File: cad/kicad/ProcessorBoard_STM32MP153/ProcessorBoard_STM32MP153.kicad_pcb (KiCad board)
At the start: 6 copper layers, 49.7 x 49.6 mm, 140 parts, among them IC301 STPMIC1BPQR, J301 Conn_01x01_Pin, J501 SFP, Q501 MMBTA92, Q502 MMBT5551L, Q503 MMBT5551L, Q504 MMBT5551L, Q505 MMBT5551L, Q506 MMBTA92, Q507 MMBT5551L, Q508 MMBTA92, Q509 MMBTA92, SW201 SW_DIP_x03, U201 STM32MP153CACx, U402 W97AH6NBVAxx, U501 DSC6101HL3B-025.0000, U502 TXS0102DCU, X201 ECS-3225MVQ-240-CN-TR, X501 RTL8211FS(I)-xx-xx

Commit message: boo womp 10000
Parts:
- moved R207 104.9 mm to (182.1, 76.7)
- moved C504 97.3 mm to (185.9, 75.8)
- moved C601 93.8 mm to (182.1, 69.1)
- moved C602 93.8 mm to (182.1, 71.6)
- moved L601 93.8 mm to (186.9, 69.8)
- moved C603 93.8 mm to (182.1, 74.2)
- moved R601 92.6 mm to (182.1, 79.2)
- moved R602 92.6 mm to (182.1, 81.7)
- moved U601 13.1 mm to (186.0, 73.3)

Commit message: found reference schematic :he he he ha:
coincidence using the same chip !? am i tweaking or tamale-n brap
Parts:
- removed C505: 100n, Capacitor_SMD:C_0402_1005Metric_Pad0.74x0.62mm_HandSolder
- removed C601, C602, C603: 10u, Capacitor_SMD:C_0603_1608Metric_Pad1.08x0.95mm_HandSolder
- removed L601: 1u, Inductor_SMD:L_1008_2520Metric_Pad1.43x2.20mm_HandSolder
- removed Q501, Q506, Q508, Q509: MMBTA92, Package_TO_SOT_SMD:SOT-23
- removed Q502, Q503, Q504, Q505, Q507: MMBT5551L, Package_TO_SOT_SMD:SOT-23
- removed R504: 240, Capacitor_SMD:C_0402_1005Metric_Pad0.74x0.62mm_HandSolder
- removed R601: 45.3k, Resistor_SMD:R_0603_1608Metric_Pad0.98x0.95mm_HandSolder
- removed R602: 10k, Resistor_SMD:R_0603_1608Metric_Pad0.98x0.95mm_HandSolder
- removed U501: DSC6101HL3B-025.0000, Package_LGA:VLGA-4_2x2.5mm_P1.65mm
- removed U601: ~, Package_TO_SOT_SMD:SOT-563
- added C514: 4.7u, Capacitor_SMD:C_0402_1005Metric_Pad0.74x0.62mm_HandSolder, F.Cu at (182.4, 90.2)
- added C515: 4.7u, Capacitor_SMD:C_0402_1005Metric_Pad0.74x0.62mm_HandSolder, F.Cu at (142.1, 52.1)
- added C516: 4.7u, Capacitor_SMD:C_0402_1005Metric_Pad0.74x0.62mm_HandSolder, F.Cu at (142.1, 54.1)
- added C517: 1n, Capacitor_SMD:C_0402_1005Metric_Pad0.74x0.62mm_HandSolder, F.Cu at (182.4, 92.2)
- added D502: LED_ABGR, LED_SMD:LED_ASMB-KTF0-0A306, F.Cu at (154.9, 50.9)
- added D503: LED_ABGR, LED_SMD:LED_ASMB-KTF0-0A306, F.Cu at (154.9, 54.5)
- added R515: 330, Resistor_SMD:R_0603_1608Metric_Pad0.98x0.95mm_HandSolder, F.Cu at (150.6, 52.9)
- added R516: 240, Capacitor_SMD:C_0402_1005Metric_Pad0.74x0.62mm_HandSolder, F.Cu at (142.1, 58.0)
- added R517: 240, Capacitor_SMD:C_0402_1005Metric_Pad0.74x0.62mm_HandSolder, F.Cu at (142.1, 60.0)
- added R518: 10k, Resistor_SMD:R_0603_1608Metric_Pad0.98x0.95mm_HandSolder, F.Cu at (150.6, 55.4)
- added R519: 5.6k, Resistor_SMD:R_0805_2012Metric_Pad1.20x1.40mm_HandSolder, F.Cu at (146.1, 59.5)
- added R520: 0, Resistor_SMD:R_0603_1608Metric, B.Cu at (169.3, 84.0)
- added U503: SN74LVC07AD, __WM_Local:D0014A_M, F.Cu at (145.2, 43.7)
- added U504: SN74LVC07AD, __WM_Local:D0014A_M, F.Cu at (154.6, 43.7)
- C233, C501, R202, R203, R204, X201: moved to B.Cu
- L502, L503: footprint Inductor_SMD:L_1008_2520Metric_Pad1.43x2.20mm_HandSolder -> Inductor_SMD:L_0805_2012Metric_Pad1.05x1.20mm_HandSolder
- R501: value 5.6k -> 100; footprint Resistor_SMD:R_0805_2012Metric_Pad1.20x1.40mm_HandSolder -> Resistor_SMD:R_0402_1005Metric
- R503: value 330 -> 5.6k; footprint Resistor_SMD:R_0603_1608Metric_Pad0.98x0.95mm_HandSolder -> Resistor_SMD:R_0805_2012Metric_Pad1.20x1.40mm_HandSolder
- R505: value 240 -> 2.49k; footprint Capacitor_SMD:C_0402_1005Metric_Pad0.74x0.62mm_HandSolder -> Resistor_SMD:R_0603_1608Metric_Pad0.98x0.95mm_HandSolder
- moved R502 104.7 mm to (146.1, 50.6)
- moved R202 95.5 mm to (174.1, 86.8)
- moved C502 92.6 mm to (176.5, 78.6), turned to -45 degrees
- moved R505 92.4 mm to (150.6, 50.4)
- moved C233 92.3 mm to (171.7, 89.1), turned to -90 degrees
- moved R503 89.5 mm to (146.1, 53.6)
- moved L501 88.4 mm to (173.8, 81.2), turned to 45 degrees
- moved C501 84.1 mm to (169.7, 85.3), turned to 180 degrees
- moved C503 82.7 mm to (173.1, 88.8)
- moved R501 66.3 mm to (165.8, 80.6), turned to 45 degrees
- moved R203 42.0 mm to (170.4, 90.4), turned to 90 degrees
- moved R204 41.0 mm to (171.7, 86.8), turned to -90 degrees
- moved X201 40.0 mm to (174.2, 89.5), turned to 180 degrees
- moved L503 13.9 mm to (159.5, 53.3)
- moved L502 12.9 mm to (159.5, 50.5)
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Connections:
- net Net-(C502-Pad1) renamed /SPF/ir_1v0
- net Net-(J501-TD+) renamed /SPF/SERDES_O_P
- net Net-(J501-TD-) renamed /SPF/SERDES_O_N
- net Net-(X501-REG_OUT) renamed /SPF/ir_out
- J501 pad 12: Net-(J501-RD-) -> /SPF/SERDES_I_N
- J501 pad 13: Net-(J501-RD+) -> /SPF/SERDES_I_P
- R501 pad 1: GND -> /SPF/SERDES_I_N
- R501 pad 2: /SPF/LED_{1} -> /SPF/SERDES_I_P
- R502 pad 1: /SPF/sfp.3v3 -> /SPF/LED_{2}
- R502 pad 2: /SPF/LED_{2} -> /SPF/sfp.3v3
- R503 pad 1: Net-(Q501-E) -> /sfp.rxd1
- R503 pad 2: Net-(D501-RK) -> /SPF/sfp.V_{io}
- R505 pad 1: Net-(Q501-E) -> Net-(X501-RSET)
- R505 pad 2: Net-(D501-BK) -> GND
- U201 pad AA1: unconnected-(U201-PG14-PadAA1) -> /sfp.txd1
- U201 pad AA2: unconnected-(U201-PG13-PadAA2) -> /sfp.txd0
- U201 pad AA4: unconnected-(U201-PA1-PadAA4) -> /sfp.rxc
- U201 pad AA6: unconnected-(U201-PC1-PadAA6) -> /sfp.mdc
- U201 pad AB2: unconnected-(U201-PG4-PadAB2) -> /sfp.txc
- U201 pad AB7: unconnected-(U201-PC5-PadAB7) -> /sfp.rxd1
- U201 pad AB8: unconnected-(U201-PA7-PadAB8) -> /sfp.rxctl
- U201 pad AC3: unconnected-(U201-PA2-PadAC3) -> /sfp.mdio
- U201 pad AC7: unconnected-(U201-PC4-PadAC7) -> /sfp.rxd0
- U201 pad K4: unconnected-(U201-PG12-PadK4) -> /sfp.phy.int#
- U201 pad W4: unconnected-(U201-PH7-PadW4) -> /sfp.rxd3
- U201 pad Y1: unconnected-(U201-PE2-PadY1) -> /sfp.txd3
- U201 pad Y11: unconnected-(U201-PH6-PadY11) -> /sfp.rxd2
- U201 pad Y2: unconnected-(U201-PC2-PadY2) -> /sfp.txd2
- U201 pad Y6: unconnected-(U201-PG5-PadY6) -> /sfp.phymac_frclk_125
- U201 pad Y7: unconnected-(U201-PG11-PadY7) -> /sfp.txctl
- U201 pad Y8: unconnected-(U201-PB5-PadY8) -> /sfp.macphy_clk_25
- X501 pad 13: unconnected-(X501-PHY_RSTB#-Pad13) -> /sfp.phy.reset#
- X501 pad 14: unconnected-(X501-MDC-Pad14) -> /sfp.mdc
- X501 pad 15: unconnected-(X501-MDIO-Pad15) -> /sfp.mdio
- X501 pad 16: unconnected-(X501-TXD_{3}-Pad16) -> /sfp.txd3
- X501 pad 17: unconnected-(X501-TXD_{2}-Pad17) -> /sfp.txd2
- X501 pad 18: unconnected-(X501-TXD_{1}-Pad18) -> /sfp.txd1
- X501 pad 19: unconnected-(X501-TXD_{0}-Pad19) -> /sfp.txd0
- X501 pad 20: unconnected-(X501-TXCTL-Pad20) -> /sfp.txctl
- X501 pad 21: unconnected-(X501-TXCLK-Pad21) -> /sfp.txc
- X501 pad 23: unconnected-(X501-CFG_{mode2}-Pad23) -> /sfp.rxd3
- X501 pad 24: unconnected-(X501-CFG_{mode1}-Pad24) -> /sfp.rxd2
- X501 pad 25: unconnected-(X501-CFG_{mode0}-Pad25) -> /sfp.rxd1
- X501 pad 26: unconnected-(X501-RXDLY-Pad26) -> /sfp.rxd0
- X501 pad 27: unconnected-(X501-PHYAD_{2}-Pad27) -> /sfp.rxctl
- X501 pad 28: unconnected-(X501-PHYAD_{1}-Pad28) -> /sfp.rxc
- X501 pad 29: unconnected-(X501-DV_{dd}_RG-Pad29) -> /SPF/sfp.V_{io}
- X501 pad 33: unconnected-(X501-PTP_CLKIN/GPIO_{0}-Pad33) -> Net-(X501-PTP_CLKIN/GPIO_{0})
- X501 pad 34: unconnected-(X501-INTB/PMEB-Pad34) -> /sfp.phy.int#
- X501 pad 35: unconnected-(X501-PHYAD_{0}-Pad35) -> /SPF/LED_{0}
- X501 pad 38: Net-(J501-RD+) -> /SPF/SERDES_I_P
- X501 pad 39: Net-(J501-RD-) -> /SPF/SERDES_I_N
- X501 pad 44: unconnected-(X501-CLKOUT-Pad44) -> /sfp.phymac_frclk_125
- X501 pad 46: /SPF/xtal_out -> /sfp.macphy_clk_25
- X501 pad 48: /SPF/reset -> Net-(X501-RSET)
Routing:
- net Net-(X201-V_{dd}): track 0.00 -> 2.61 mm
- net Net-(X201-EN): track 0.00 -> 1.81 mm
- net Net-(X501-PTP_CLKIN/GPIO_{0}): track 0.00 -> 0.74 mm
- net GND: track 2.57 -> 2.93 mm, vias 33 -> 35
- net /sfp.rxd0: track 0.00 -> 0.35 mm, vias 0 -> 1
- net /sfp.mdio: track 0.00 -> 0.31 mm, vias 0 -> 1
- net /sfp.phymac_frclk_125: track 0.00 -> 0.31 mm, vias 0 -> 1
- net /sfp.txd1: track 0.00 -> 0.31 mm, vias 0 -> 1
- net /sfp.phy.int#: track 0.00 -> 0.31 mm, vias 0 -> 1
- net /sfp.macphy_clk_25: track 0.00 -> 0.31 mm, vias 0 -> 1
- net /sfp.rxd3: track 0.00 -> 0.31 mm, vias 0 -> 1
- net /sfp.rxc: track 0.00 -> 0.31 mm, vias 0 -> 1
- net /sfp.rxctl: track 0.00 -> 0.31 mm, vias 0 -> 1
- net /sfp.mdc: track 0.00 -> 0.31 mm, vias 0 -> 1
- net /sfp.txd0: track 0.00 -> 0.31 mm, vias 0 -> 1
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
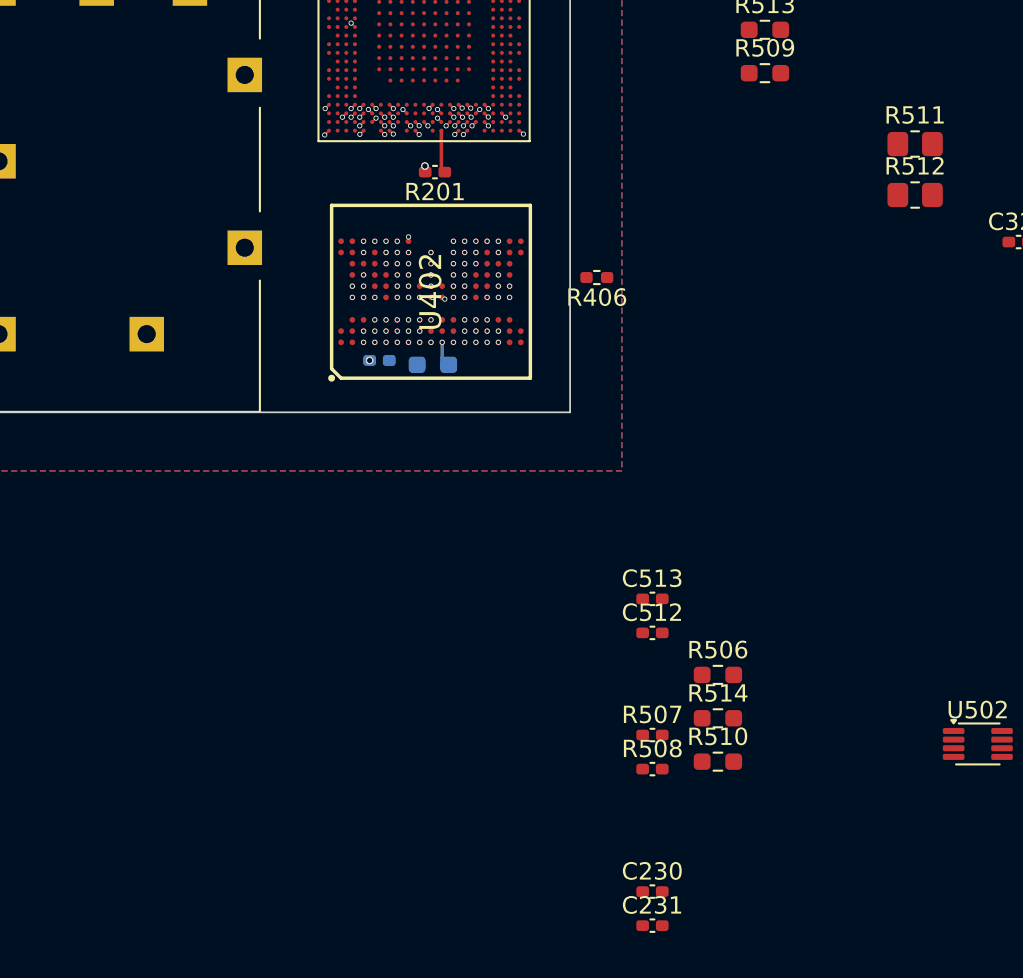
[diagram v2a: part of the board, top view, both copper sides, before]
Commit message: i forgor track spacing :(
need to redo ddr
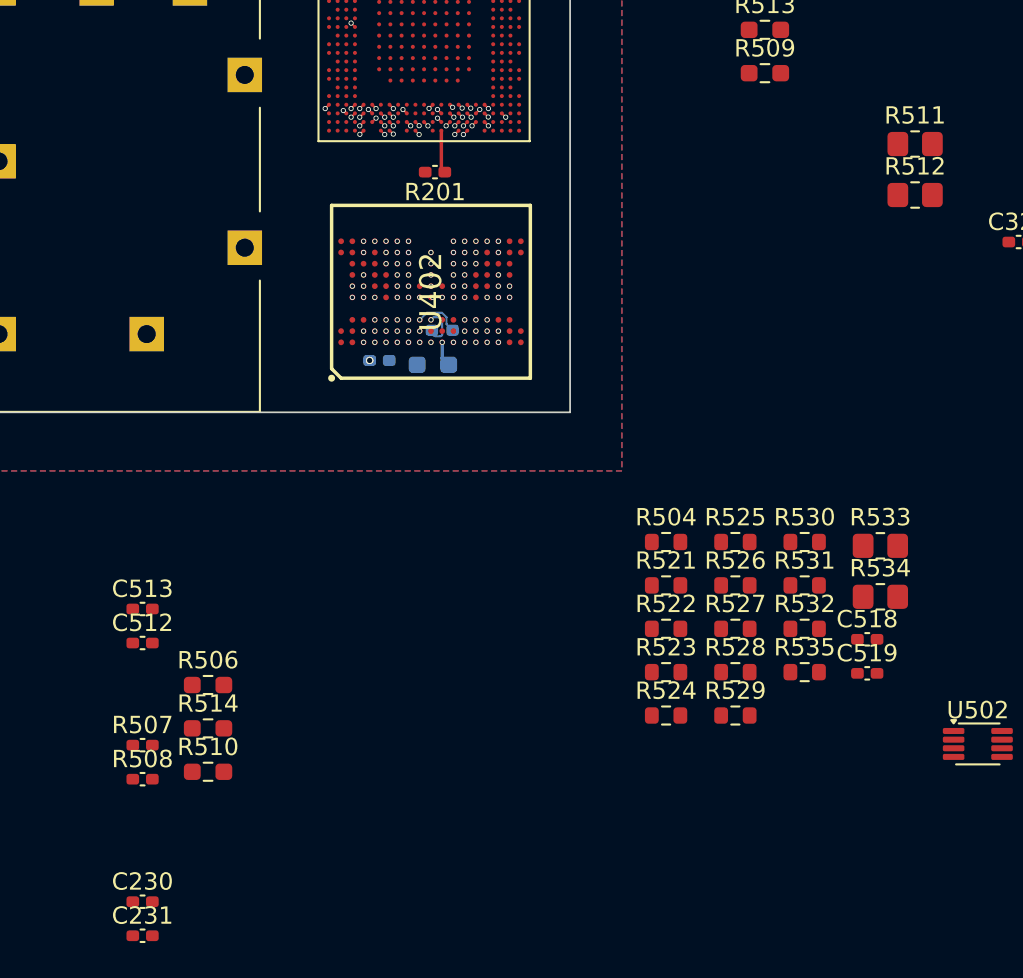
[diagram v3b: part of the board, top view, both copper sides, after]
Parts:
- added C518: 100n, Capacitor_SMD:C_0402_1005Metric_Pad0.74x0.62mm_HandSolder, F.Cu at (197.2, 132.7)
- added C519: 100n, Capacitor_SMD:C_0402_1005Metric_Pad0.74x0.62mm_HandSolder, F.Cu at (197.2, 134.7)
- added R504: 22, Resistor_SMD:R_0603_1608Metric, F.Cu at (185.6, 127.1)
- added R521: 22, Resistor_SMD:R_0603_1608Metric, F.Cu at (185.6, 129.6)
- added R522: 22, Resistor_SMD:R_0603_1608Metric, F.Cu at (185.6, 132.1)
- added R523: 22, Resistor_SMD:R_0603_1608Metric, F.Cu at (185.6, 134.6)
- added R524: 22, Resistor_SMD:R_0603_1608Metric, F.Cu at (185.6, 137.1)
- added R525: 22, Resistor_SMD:R_0603_1608Metric, F.Cu at (189.6, 127.1)
- added R526: 22, Resistor_SMD:R_0603_1608Metric, F.Cu at (189.6, 129.6)
- added R527: 22, Resistor_SMD:R_0603_1608Metric, F.Cu at (189.6, 132.1)
- added R528: 22, Resistor_SMD:R_0603_1608Metric, F.Cu at (189.6, 134.6)
- added R529: 22, Resistor_SMD:R_0603_1608Metric, F.Cu at (189.6, 137.1)
- added R530: 22, Resistor_SMD:R_0603_1608Metric, F.Cu at (193.6, 127.1)
- added R531: 22, Resistor_SMD:R_0603_1608Metric, F.Cu at (193.6, 129.6)
- added R532: 22, Resistor_SMD:R_0603_1608Metric, F.Cu at (193.6, 132.1)
- added R533: 5.6k, Resistor_SMD:R_0805_2012Metric_Pad1.20x1.40mm_HandSolder, F.Cu at (198.0, 127.3)
- added R534: 5.6k, Resistor_SMD:R_0805_2012Metric_Pad1.20x1.40mm_HandSolder, F.Cu at (198.0, 130.3)
- added R535: 22, Resistor_SMD:R_0603_1608Metric, F.Cu at (193.6, 134.6)
- R406: moved to B.Cu
- moved C230 29.5 mm to (155.3, 147.9)
- moved C231 29.5 mm to (155.3, 149.9)
- moved C512 29.5 mm to (155.3, 132.9)
- moved C513 29.5 mm to (155.3, 131.0)
- moved R506 29.5 mm to (159.1, 135.4)
- moved R507 29.5 mm to (155.3, 138.9)
- moved R508 29.5 mm to (155.3, 140.8)
- moved R510 29.5 mm to (159.1, 140.4)
- moved R514 29.5 mm to (159.1, 137.9)
- moved R406 9.45 mm to (172.6, 114.8), turned to 0 degrees
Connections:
- C501 pad 1: /SPF/sfp.3v3 -> GND
- C501 pad 2: GND -> /3v3
- C503 pad 2: /SPF/sfp.3v3 -> /3v3
- C510 pad 1: /SPF/sfp.3v3 -> /3v3
- C511 pad 1: /SPF/sfp.3v3 -> /3v3
- C512 pad 1: /SPF/sfp.V_{io} -> /V_{dd_IO}
- C513 pad 1: /SPF/sfp.3v3 -> /3v3
- C514 pad 2: /SPF/sfp.V_{io} -> /V_{dd_IO}
- C515 pad 1: /SPF/sfp.3v3 -> /3v3
- C516 pad 1: /SPF/sfp.V_{io} -> /V_{dd_IO}
- C517 pad 2: /SPF/sfp.V_{io} -> /V_{dd_IO}
- D502 pad 1: /SPF/sfp.3v3 -> /3v3
- D503 pad 1: /SPF/sfp.3v3 -> /3v3
- L502 pad 1: /SPF/sfp.3v3 -> /3v3
- L503 pad 1: /SPF/sfp.3v3 -> /3v3
- R502 pad 2: /SPF/sfp.3v3 -> /3v3
- R503 pad 1: /sfp.rxd1 -> /V_{dd_IO}
- R503 pad 2: /SPF/sfp.V_{io} -> Net-(X501-CFG_{mode0})
- R511 pad 2: /SPF/sfp.3v3 -> /3v3
- R512 pad 1: /SPF/sfp.3v3 -> /3v3
- R513 pad 1: /SPF/sfp.3v3 -> /3v3
- R514 pad 1: /SPF/sfp.3v3 -> /3v3
- R518 pad 2: /SPF/sfp.3v3 -> /3v3
- U402 pad E8: /ddr.d12 -> /ddr.d13
- U402 pad F8: /ddr.d10 -> /ddr.d14
- U402 pad F9: /ddr.d13 -> /ddr.d12
- U402 pad G7: /ddr.d14 -> /ddr.d10
- U502 pad 3: /SPF/sfp.V_{io} -> /V_{dd_IO}
- U502 pad 6: /SPF/sfp.V_{io} -> /V_{dd_IO}
- U502 pad 7: /SPF/sfp.3v3 -> /3v3
- U503 pad 14: /SPF/sfp.3v3 -> /3v3
- U504 pad 14: /SPF/sfp.V_{io} -> /V_{dd_IO}
- X501 pad 1: /SPF/sfp.3v3 -> /3v3
- X501 pad 12: /SPF/sfp.3v3 -> /3v3
- X501 pad 14: /sfp.mdc -> Net-(X501-MDC)
- X501 pad 16: /sfp.txd3 -> Net-(X501-TXD_{3})
- X501 pad 17: /sfp.txd2 -> Net-(X501-TXD_{2})
- X501 pad 18: /sfp.txd1 -> Net-(X501-TXD_{1})
- X501 pad 19: /sfp.txd0 -> Net-(X501-TXD_{0})
- X501 pad 20: /sfp.txctl -> Net-(X501-TXCTL)
- X501 pad 21: /sfp.txc -> Net-(X501-TXCLK)
- X501 pad 23: /sfp.rxd3 -> Net-(X501-CFG_{mode2})
- X501 pad 24: /sfp.rxd2 -> Net-(X501-CFG_{mode1})
- X501 pad 25: /sfp.rxd1 -> Net-(X501-CFG_{mode0})
- X501 pad 26: /sfp.rxd0 -> Net-(X501-RXDLY)
- X501 pad 27: /sfp.rxctl -> Net-(X501-PHYAD_{2})
- X501 pad 28: /sfp.rxc -> Net-(X501-PHYAD_{1})
- X501 pad 29: /SPF/sfp.V_{io} -> /V_{dd_IO}
- X501 pad 30: /SPF/sfp.3v3 -> /3v3
- X501 pad 31: /SPF/sfp.3v3 -> /3v3
- X501 pad 44: /sfp.phymac_frclk_125 -> Net-(X501-CLKOUT)
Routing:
- net /ddr.a3: track 24.5 -> 0.31 mm
- net /ddr.d9: track 24.4 -> 0.31 mm
- net /ddr.CSn: track 23.1 -> 0.32 mm
- net /ddr.a1: track 23.1 -> 0.31 mm
- net /ddr.CKE: track 24.6 -> 1.77 mm
- net /ddr.d13: track 23.1 -> 0.30 mm
- net /ddr.a0: track 23.1 -> 0.30 mm
- net /ddr.d8: track 23.0 -> 0.31 mm
- net /ddr.d10: track 23.0 -> 0.31 mm
- net /ddr.CLK_P: track 24.5 -> 2.78 mm
- net /ddr.CLK_N: track 24.4 -> 3.04 mm
- net /ddr.d7: track 24.5 -> 9.34 mm
- net /ddr.d12: track 24.4 -> 10.3 mm
- net /ddr.d0: track 23.0 -> 9.03 mm
- net /ddr.d1: track 24.4 -> 10.4 mm
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
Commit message: ddr shuffle maxxing round 2
mostly hitting the 3w and 4w spacing. one must hope. #hope
ive disabled DRC for optimal routing experience . ching chong over clank ckong any day(until i get the good stuff) has nothing on the sweat shop.
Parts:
- moved R507 80.9 mm to (170.5, 59.4)
- moved R508 80.9 mm to (170.5, 61.4)
- moved R506 80.9 mm to (174.3, 55.9)
- moved R510 80.9 mm to (174.3, 60.9)
- moved R514 80.9 mm to (174.3, 58.4)
- moved C518 57.9 mm to (139.4, 135.4)
- moved C519 57.9 mm to (139.4, 137.4)
- moved R504 57.9 mm to (127.8, 129.8)
- moved R521 57.9 mm to (127.8, 132.3)
- moved R522 57.9 mm to (127.8, 134.8)
- moved R523 57.9 mm to (127.8, 137.3)
- moved R524 57.9 mm to (127.8, 139.8)
- moved R525 57.9 mm to (131.8, 129.8)
- moved R526 57.9 mm to (131.8, 132.3)
- moved R527 57.9 mm to (131.8, 134.8)
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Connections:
- U402 pad E8: /ddr.d13 -> /ddr.d10
- U402 pad F6: /ddr.d15 -> /ddr.d12
- U402 pad F7: /ddr.d11 -> /ddr.d13
- U402 pad F8: /ddr.d14 -> /ddr.d11
- U402 pad F9: /ddr.d12 -> /ddr.d14
- U402 pad G7: /ddr.d10 -> /ddr.d8
- U402 pad G8: /ddr.d8 -> /ddr.d15
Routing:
- net /ddr.d8: track 0.31 -> 27.6 mm
- net /ddr.CKE: track 1.77 -> 27.4 mm
- net /ddr.a0: track 0.30 -> 24.1 mm
- net /ddr.CLK_P: track 2.78 -> 23.0 mm
- net /ddr.CLK_N: track 3.04 -> 22.7 mm
- net /ddr.a1: track 0.31 -> 17.5 mm
- net /ddr.d10: track 0.31 -> 15.5 mm
- net /ddr.CSn: track 0.32 -> 14.1 mm
- net /ddr.a3: track 0.31 -> 13.9 mm
- net /ddr.d9: track 0.31 -> 13.2 mm
- net /ddr.d6: track 14.6 -> 24.0 mm
- net /ddr.d13: track 0.30 -> 8.74 mm
- net /ddr.s1_P: track 12.7 -> 20.5 mm
- net /ddr.s1_N: track 12.8 -> 20.5 mm
- net /ddr.s0_P: track 11.9 -> 19.5 mm
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
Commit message: ddr spaced out 3w 4w binding
smooth as a babys bum or what ever else old folks say
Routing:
- net /ddr.d5: track 11.6 -> 35.2 mm
- net /ddr.d13: track 8.74 -> 31.9 mm
- net /ddr.d7: track 10.4 -> 33.4 mm
- net /ddr.m0: track 10.9 -> 33.5 mm
- net /ddr.d1: track 11.3 -> 32.0 mm
- net /ddr.d3: track 12.9 -> 33.3 mm
- net /ddr.d9: track 13.2 -> 33.4 mm
- net /ddr.m1: track 13.5 -> 33.4 mm
- net /ddr.d0: track 12.9 -> 32.0 mm
- net /ddr.a3: track 13.9 -> 32.1 mm
- net /ddr.CSn: track 14.1 -> 32.0 mm
- net /ddr.d12: track 15.2 -> 31.9 mm
- net /ddr.d10: track 15.5 -> 32.0 mm
- net /ddr.d14: track 17.6 -> 33.2 mm
- net /ddr.d4: track 17.9 -> 33.3 mm
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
